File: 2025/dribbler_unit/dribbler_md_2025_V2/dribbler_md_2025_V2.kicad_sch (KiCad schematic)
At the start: 86 parts, among them J1 Conn_01x02_Pin, J2 Conn_01x04_Pin, J3 Conn_01x05_Pin, J4 Conn_01x07_Pin, SW1 SW_Wuerth_450301014042, SW2 SW_MEC_5E, SW3 SW_Wuerth_450301014042, SW4 SW_MEC_5E, U1 MAX3051, U2 STS8DN3LLH5, U3 STS8DN3LLH5, U4 DRV8701, U5 STM32F446RETx, Y1 Crystal_GND2

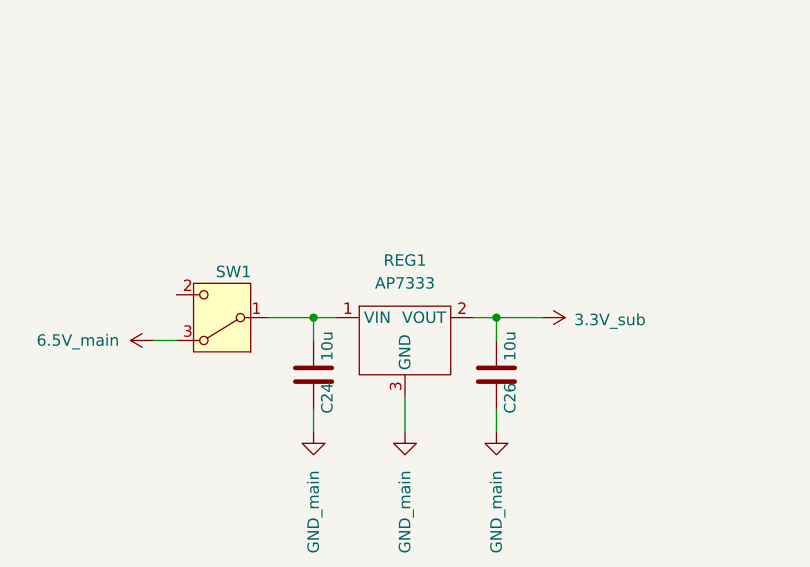
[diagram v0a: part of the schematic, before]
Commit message: シルク削除＆追加  3Dデータ出力
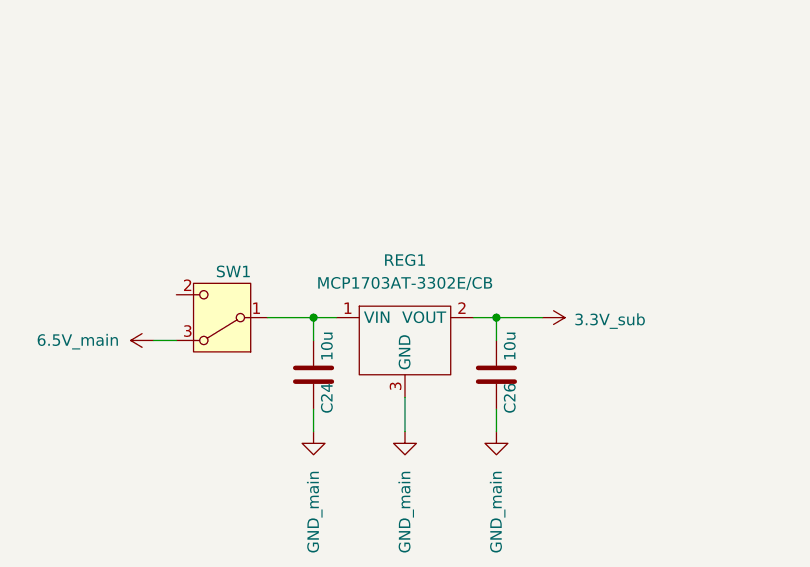
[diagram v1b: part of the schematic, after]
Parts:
- REG1: value AP7333 -> MCP1703AT-3302E/CB
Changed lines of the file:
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@@
 			)
 		)
-		(property "Value" "AP7333"
+		(property "Value" " MCP1703AT-3302E/CB"
 			(at 137.16 218.44 0)
 			(effects

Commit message: 抵抗を追加
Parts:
- added R30, R31: 0, Resistor_SMD:R_0603_1608Metric_Pad0.98x0.95mm_HandSolder, symbol Device:R
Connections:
- net GND_log: now also R30.2, R31.2
- net GND_main: now also R30.1, R31.1
